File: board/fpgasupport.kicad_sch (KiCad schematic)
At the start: 1 part, among them U4 XC7S15-1FTGB196C

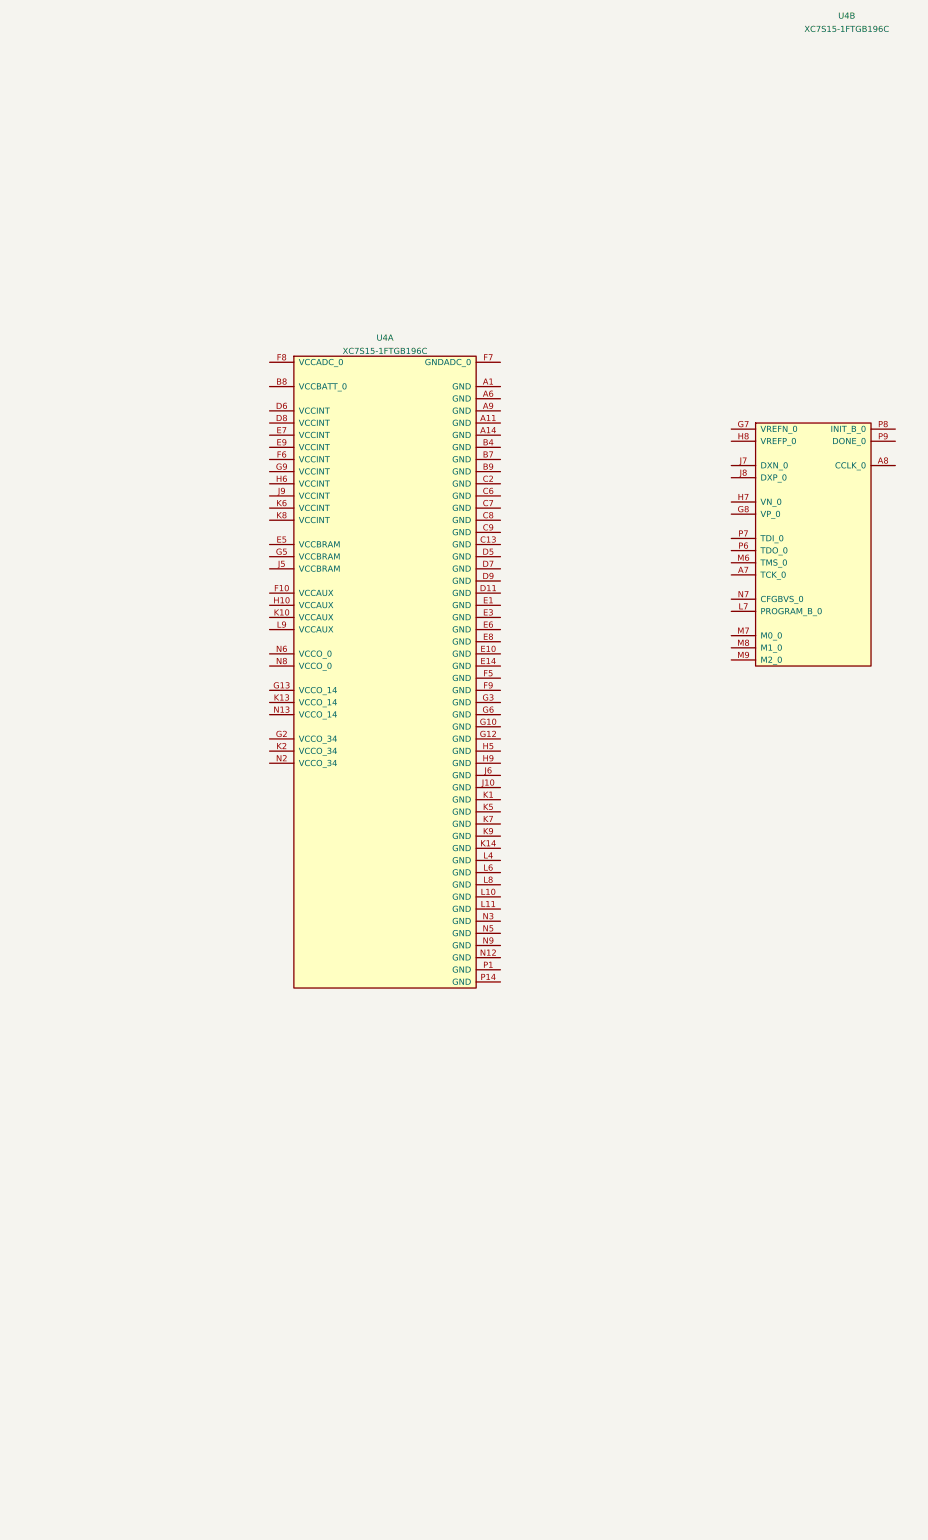
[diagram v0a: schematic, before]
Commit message: Continued initial schematic capture
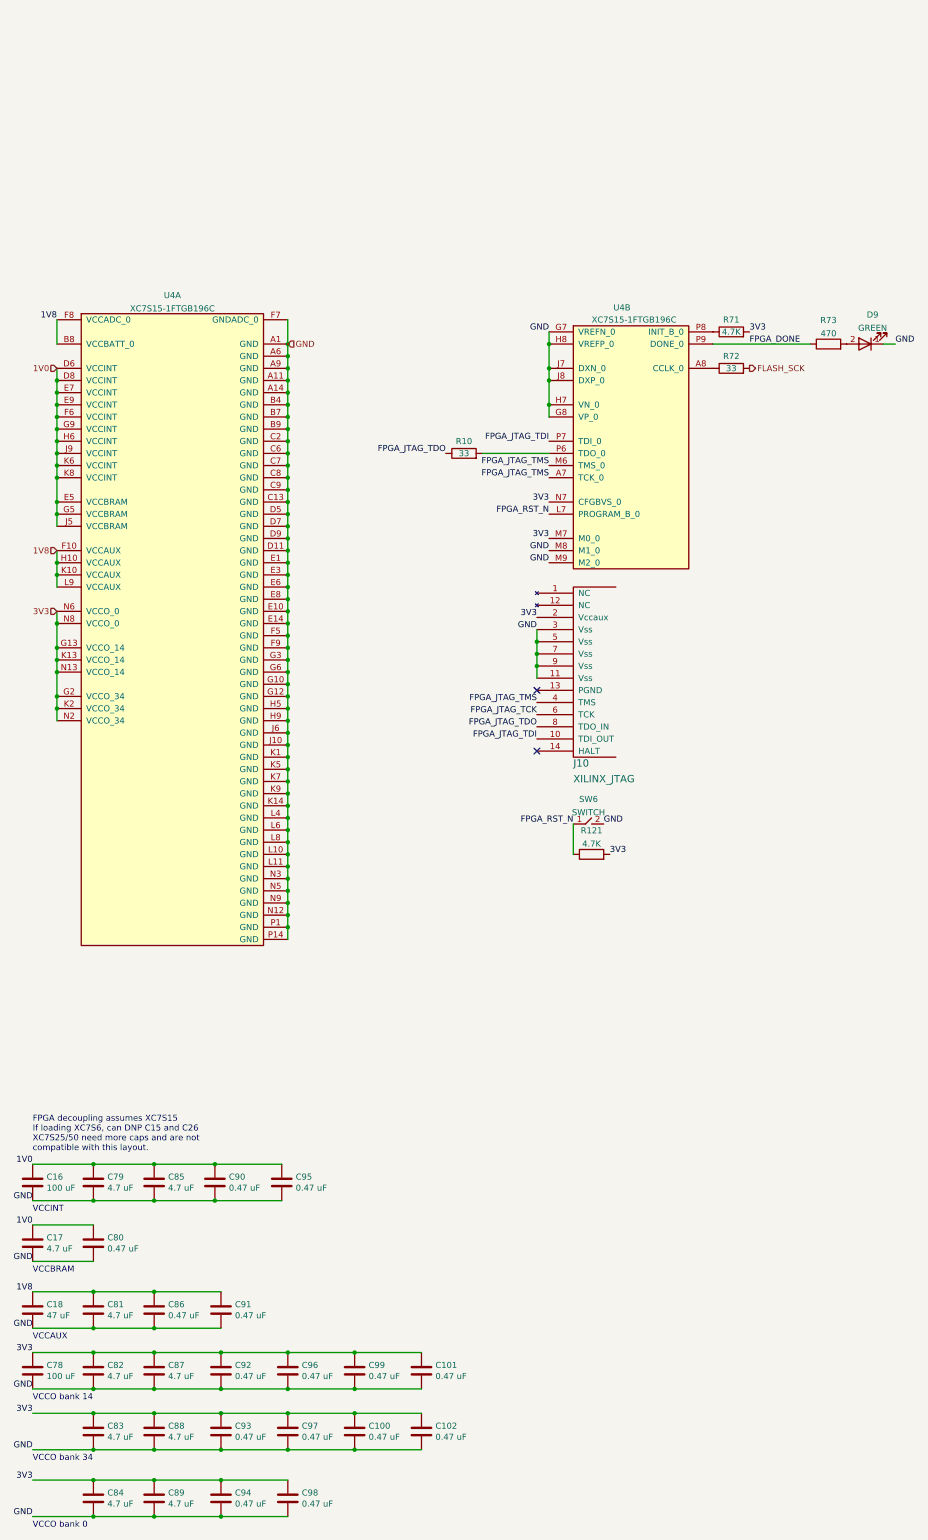
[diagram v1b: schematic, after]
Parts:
- added C100, C101, C102, C80, C86, C90, C91, C92, C93, C94, C95, C96, C97, C98, C99: 0.47 uF, azonenberg_pcb:EIA_0402_CAP_NOSILK, symbol device:C
- added C16, C78: 100 uF, azonenberg_pcb:EIA_1206_CAP_NOSILK, symbol device:C
- added C17, C79, C81, C82, C83, C84, C85, C87, C88, C89: 4.7 uF, azonenberg_pcb:EIA_0603_CAP_NOSILK, symbol device:C
- added C18: 47 uF, azonenberg_pcb:EIA_1206_CAP_NOSILK, symbol device:C
- added D9: GREEN, azonenberg_pcb:EIA_0603_LED, symbol device:LED
- added J10: XILINX_JTAG, azonenberg_pcb:XILINX_JTAG_PTH_MOLEX_0878311420, symbol xilinx-azonenberg:XILINX_JTAG
- added R10, R72: 33, azonenberg_pcb:EIA_0402_RES_NOSILK, symbol device:R
- added R121: 4.7K, symbol device:R
- added R71: 4.7K, azonenberg_pcb:EIA_0402_RES_NOSILK, symbol device:R
- added R73: 470, azonenberg_pcb:EIA_0402_RES_NOSILK, symbol device:R
- added SW6: SWITCH, symbol passive-azonenberg:SWITCH
- U4: footprint (none) -> azonenberg_pcb:BGA_196_15x15_FULLARRAY_1MM_FTGB196
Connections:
- net FPGA_JTAG_TMS: now reaches U4.A7 (TCK_0)
- net FPGA_JTAG_TMS: now also U4.M6 (TMS_0), J10.4 (TMS)
- net at U4.A8 (CCLK_0): now also R72.1
- net GND: now reaches U4.G7 (VREFN_0)
- net GND: now also U4.A1 (GND), U4.A11 (GND), U4.A14 (GND), U4.A6 (GND), U4.A9 (GND), U4.B4 (GND), U4.B7 (GND), U4.B9 (GND), U4.C13 (GND), U4.C2 (GND), U4.C6 (GND), U4.C7 (GND), U4.C8 (GND), U4.C9 (GND), U4.D11 (GND), U4.D5 (GND), U4.D7 (GND), U4.D9 (GND), U4.E1 (GND), U4.E10 (GND), U4.E14 (GND), U4.E3 (GND), U4.E6 (GND), U4.E8 (GND), U4.F5 (GND), U4.F7 (GNDADC_0), U4.F9 (GND), U4.G10 (GND), U4.G12 (GND), U4.G3 (GND), U4.G6 (GND), U4.G8 (VP_0), U4.H5 (GND), U4.H7 (VN_0), U4.H8 (VREFP_0), U4.H9 (GND), U4.J10 (GND), U4.J6 (GND), U4.J7 (DXN_0), U4.J8 (DXP_0), U4.K1 (GND), U4.K14 (GND), U4.K5 (GND), U4.K7 (GND), U4.K9 (GND), U4.L10 (GND), U4.L11 (GND), U4.L4 (GND), U4.L6 (GND), U4.L8 (GND), U4.M8 (M1_0), U4.M9 (M2_0), U4.N12 (GND), U4.N3 (GND), U4.N5 (GND), U4.N9 (GND), U4.P1 (GND), U4.P14 (GND), C100.2, C101.2, C102.2, C16.2, C17.2, C18.2, C78.2, C79.2, C80.2, C81.2, C82.2, C83.2, C84.2, C85.2, C86.2, C87.2, C88.2, C89.2, C90.2, C91.2, C92.2, C93.2, C94.2, C95.2, C96.2, C97.2, C98.2, C99.2, D9.1 (K), J10.11 (Vss), J10.3 (Vss), J10.5 (Vss), J10.7 (Vss), J10.9 (Vss), SW6.2
- net FPGA_RST_N: now reaches U4.L7 (PROGRAM_B_0)
- net FPGA_RST_N: now also R121.1, SW6.1
- net 3V3: now reaches U4.M7 (M0_0)
- net 3V3: now also U4.G13 (VCCO_14), U4.G2 (VCCO_34), U4.K13 (VCCO_14), U4.K2 (VCCO_34), U4.N13 (VCCO_14), U4.N2 (VCCO_34), U4.N6 (VCCO_0), U4.N7 (CFGBVS_0), U4.N8 (VCCO_0), C100.1, C101.1, C102.1, C78.1, C82.1, C83.1, C84.1, C87.1, C88.1, C89.1, C92.1, C93.1, C94.1, C96.1, C97.1, C98.1, C99.1, J10.2 (Vccaux), R121.2, R71.2
- net at U4.P6 (TDO_0): now also R10.2
- net FPGA_JTAG_TDI: now reaches U4.P7 (TDI_0)
- net FPGA_JTAG_TDI: now also J10.10 (TDI_OUT)
- net at U4.P8 (INIT_B_0): now also R71.1
- net FPGA_DONE: now reaches U4.P9 (DONE_0)
- net FPGA_DONE: now also R73.1
- net 1V8: now reaches U4.B8 (VCCBATT_0)
- net 1V8: now also U4.F10 (VCCAUX), U4.F8 (VCCADC_0), U4.H10 (VCCAUX), U4.K10 (VCCAUX), U4.L9 (VCCAUX), C18.1, C81.1, C86.1, C91.1
- net 1V0: now reaches U4.D6 (VCCINT)
- net 1V0: now also U4.D8 (VCCINT), U4.E5 (VCCBRAM), U4.E7 (VCCINT), U4.E9 (VCCINT), U4.F6 (VCCINT), U4.G5 (VCCBRAM), U4.G9 (VCCINT), U4.H6 (VCCINT), U4.J5 (VCCBRAM), U4.J9 (VCCINT), U4.K6 (VCCINT), U4.K8 (VCCINT), C16.1, C17.1, C79.1, C80.1, C85.1, C90.1, C95.1
- new net: D9.2 (A), R73.2
- new net FLASH_SCK: R72.2
- new net FPGA_JTAG_TCK: J10.6 (TCK)
- new net FPGA_JTAG_TDO: J10.8 (TDO_IN), R10.1
- no-connect marks 0 -> 2
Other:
- note added: "FPGA decoupling assumes XC7S15 If loading XC7S6, can DNP C15 and C26 XC7S25/50 need more caps and are not compatible with this layout."
- note added: "VCCAUX"
- note added: "VCCBRAM"
- note added: "VCCINT"
- note added: "VCCO bank 0"
- note added: "VCCO bank 14"
- note added: "VCCO bank 34"
- moved on the sheet: U4A, U4B

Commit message: Finished initial schematic, ready for signoff review
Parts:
- C16: footprint azonenberg_pcb:EIA_1206_CAP_NOSILK -> azonenberg_pcb:EIA_1210_CAP_NOSILK
- R121: footprint (none) -> azonenberg_pcb:EIA_0402_RES_NOSILK
- SW6: footprint (none) -> azonenberg_pcb:SWITCH_RAFI_MICON_5
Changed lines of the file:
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@@
       (effects (font (size 1.27 1.27)) (justify left))
     )
-    (property "Footprint" "azonenberg_pcb:EIA_1206_CAP_NOSILK" (id 2) (at 27.6352 204.47 0)
+    (property "Footprint" "azonenberg_pcb:EIA_1210_CAP_NOSILK" (id 2) (at 27.6352 204.47 0)
       (effects (font (size 1.27 1.27)) hide)
     )
@@
     (property "Reference" "SW6" (id 0) (at 142.875 120.5443 0))
     (property "Value" "SWITCH" (id 1) (at 142.875 123.3194 0))
-    (property "Footprint" "" (id 2) (at 142.24 125.73 0)
+    (property "Footprint" "azonenberg_pcb:SWITCH_RAFI_MICON_5" (id 2) (at 142.24 125.73 0)
       (effects (font (size 1.27 1.27)) hide)
     )
@@
     (property "Reference" "R121" (id 0) (at 143.51 127.0975 90))
     (property "Value" "4.7K" (id 1) (at 143.51 129.8726 90))
-    (property "Footprint" "" (id 2) (at 143.51 133.858 90)
-      (effects (font (size 1.27 1.27)) hide)
-    )
+    (property "Footprint" "azonenberg_pcb:EIA_0402_RES_NOSILK" (id 2) (at 143.51 133.858 90)
+      (effects (font (size 1.27 1.27)) hide)
+    )

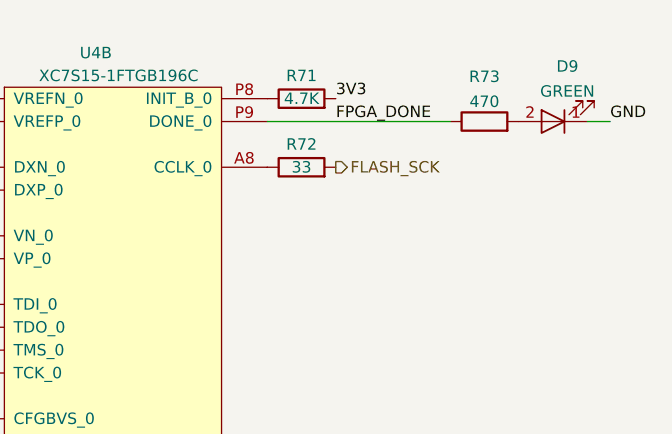
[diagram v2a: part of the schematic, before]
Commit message: Finished schematic review. Added a few more test points.
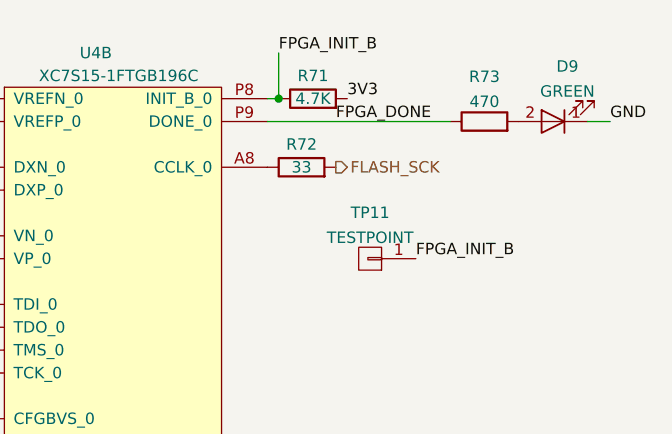
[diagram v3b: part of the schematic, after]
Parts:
- added TP11: TESTPOINT, azonenberg_pcb:TESTPOINT_SMT_0.5MM, symbol conn:CONN_01X01
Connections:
- net FPGA_INIT_B: now reaches R71.1, U4.P8 (INIT_B_0)
- net FPGA_INIT_B: now also TP11.1 (P1)
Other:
- moved on the sheet: R71
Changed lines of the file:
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@@
   (junction (at 52.07 236.22) (diameter 0) (color 0 0 0 0)
+  )
+  (junction (at 170.18 22.86) (diameter 0) (color 0 0 0 0)
   )
   (junction (at 39.37 270.51) (diameter 0) (color 0 0 0 0)
@@
     (stroke (width 0) (type default) (color 0 0 0 0))
   )
+  (wire (pts (xy 170.18 17.78) (xy 170.18 22.86))
+    (stroke (width 0) (type default) (color 0 0 0 0))
+  )
   (wire (pts (xy 52.07 223.52) (xy 39.37 223.52))
     (stroke (width 0) (type default) (color 0 0 0 0))
@@
   )
   (wire (pts (xy 80.01 96.52) (xy 80.01 99.06))
+    (stroke (width 0) (type default) (color 0 0 0 0))
+  )
+  (wire (pts (xy 168.91 22.86) (xy 170.18 22.86))
     (stroke (width 0) (type default) (color 0 0 0 0))
   )
@@
     (effects (font (size 1.27 1.27)) (justify left bottom))
   )
-  (label "3V3" (at 176.53 22.86 0)
+  (label "3V3" (at 177.8 22.86 0)
     (effects (font (size 1.27 1.27)) (justify left bottom))
   )
@@
     (effects (font (size 1.27 1.27)) (justify right bottom))
   )
+  (label "FPGA_INIT_B" (at 170.18 17.78 0)
+    (effects (font (size 1.27 1.27)) (justify left bottom))
+  )
   (label "3V3" (at 134.62 66.04 180)
     (effects (font (size 1.27 1.27)) (justify right bottom))
@@
   (label "3V3" (at 132.08 82.55 180)
     (effects (font (size 1.27 1.27)) (justify right bottom))
+  )
+  (label "FPGA_INIT_B" (at 185.42 40.64 0)
+    (effects (font (size 1.27 1.27)) (justify left bottom))
   )
   (label "FPGA_JTAG_TMS" (at 134.62 53.34 180)
@@
     (pin "2")
   )
-  (symbol (lib_id "device:R") (at 172.72 22.86 90) (unit 1)
-    (in_bom yes) (on_board yes)
-    (property "Reference" "R71" (id 0) (at 172.72 20.32 90))
-    (property "Value" "4.7K" (id 1) (at 172.72 22.86 90))
-    (property "Footprint" "azonenberg_pcb:EIA_0402_RES_NOSILK" (id 2) (at 172.72 24.638 90)
-      (effects (font (size 1.27 1.27)) hide)
-    )
-    (property "Datasheet" "" (id 3) (at 172.72 22.86 0)
+  (symbol (lib_id "device:R") (at 173.99 22.86 90) (unit 1)
+    (in_bom yes) (on_board yes)
+    (property "Reference" "R71" (id 0) (at 173.99 20.32 90))
+    (property "Value" "4.7K" (id 1) (at 173.99 22.86 90))
+    (property "Footprint" "azonenberg_pcb:EIA_0402_RES_NOSILK" (id 2) (at 173.99 24.638 90)
+      (effects (font (size 1.27 1.27)) hide)
+    )
+    (property "Datasheet" "" (id 3) (at 173.99 22.86 0)
       (effects (font (size 1.27 1.27)) hide)
     )
@@
     (pin "2")
   )
+  (symbol (lib_id "conn:CONN_01X01") (at 180.34 40.64 180) (unit 1)
+    (in_bom yes) (on_board yes) (fields_autoplaced)
+    (property "Reference" "TP11" (id 0) (at 180.34 35.5305 0))
+    (property "Value" "TESTPOINT" (id 1) (at 180.34 38.3056 0))
+    (property "Footprint" "azonenberg_pcb:TESTPOINT_SMT_0.5MM" (id 2) (at 180.34 40.64 0)
+      (effects (font (size 1.27 1.27)) hide)
+    )
+    (property "Datasheet" "" (id 3) (at 180.34 40.64 0)
+      (effects (font (size 1.27 1.27)) hide)
+    )
+    (pin "1")
+  )
   (symbol (lib_id "device:R") (at 193.04 25.4 90) (unit 1)

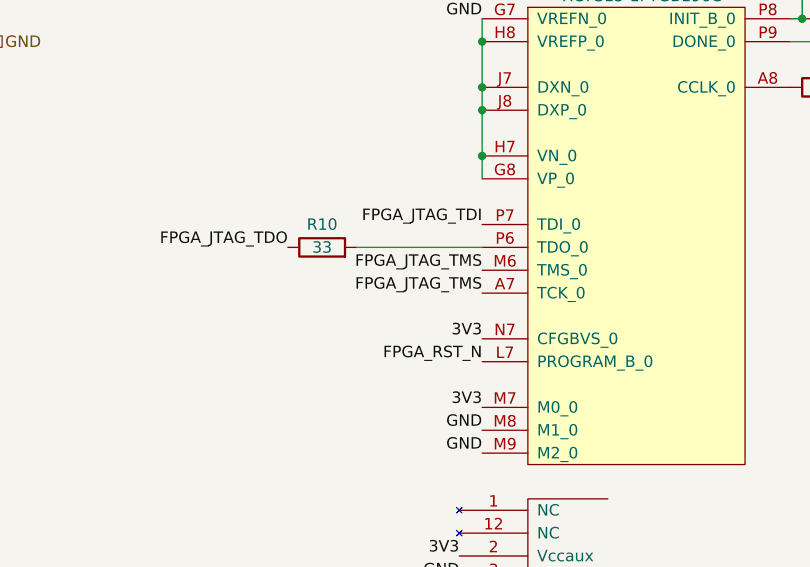
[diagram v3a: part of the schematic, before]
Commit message: Continued initial layout. First PHY fully routed including connection to FPGA. Hooked up 0402 bypass caps under FPGA. Flash is roughly placed.
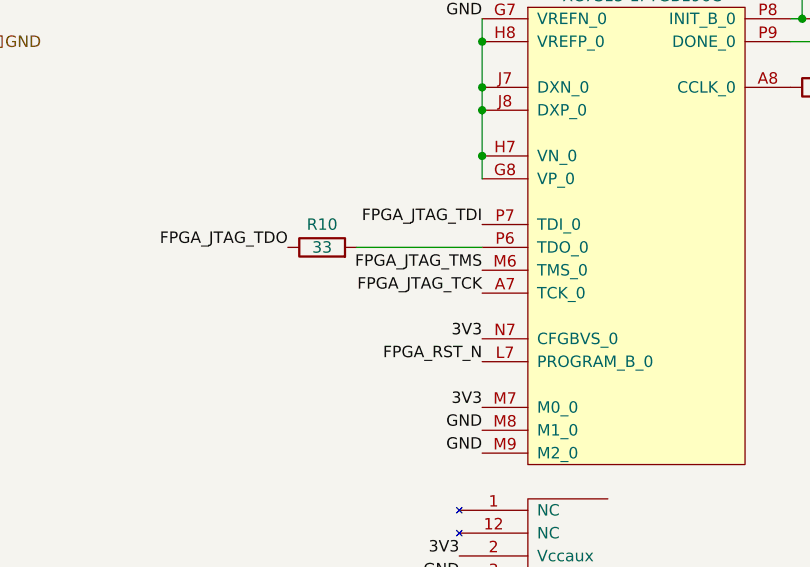
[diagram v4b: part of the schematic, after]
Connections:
- net FPGA_JTAG_TCK: now also U4.A7 (TCK_0)
- net FPGA_JTAG_TMS: no longer U4.A7 (TCK_0)
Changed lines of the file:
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@@
   (title_block
     (title "Active 10/100/1000baseT Tap")
-    (date "2022-12-20")
+    (date "2022-12-21")
     (rev "0.1")
     (company "Antikernel Labs")
@@
     (effects (font (size 1.27 1.27)) (justify left bottom))
   )
-  (label "FPGA_JTAG_TMS" (at 134.62 53.34 180)
-    (effects (font (size 1.27 1.27)) (justify right bottom))
-  )
+  (label "FPGA_JTAG_TCK" (at 134.62 53.34 180)
+    (effects (font (size 1.27 1.27)) (justify right bottom))
+  )
